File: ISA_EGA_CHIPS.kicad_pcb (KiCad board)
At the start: 2 copper layers, 131.1 x 108 mm, 67 parts, among them J1 EGA Feature Connector, J2 Light Pen, J3 RCA 1, J4 RCA 2, J6 Digital Output, J7 Bus_ISA_8bit, SW1 Configuration, U1 41464, U10 27C256, U11 82A436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

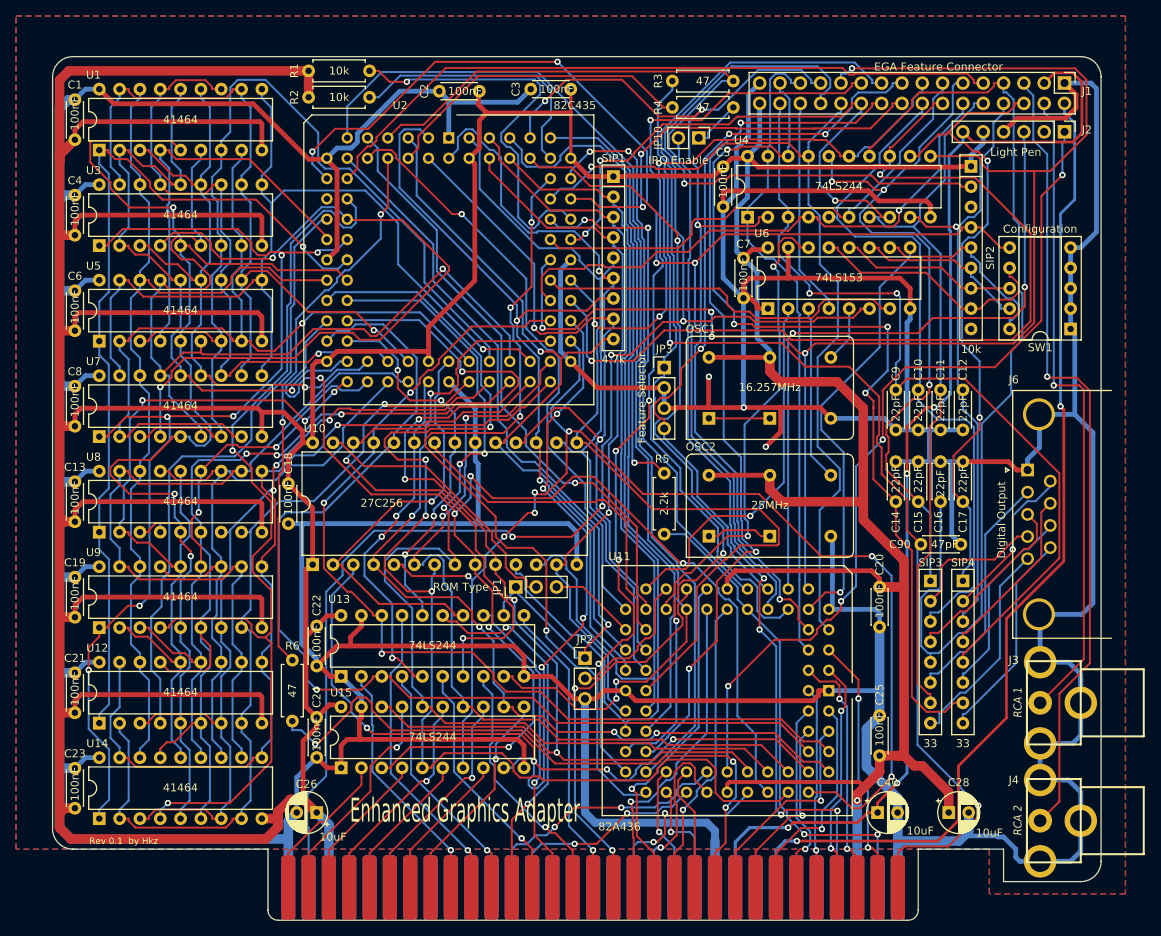
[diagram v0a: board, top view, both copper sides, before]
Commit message: Better ground plane
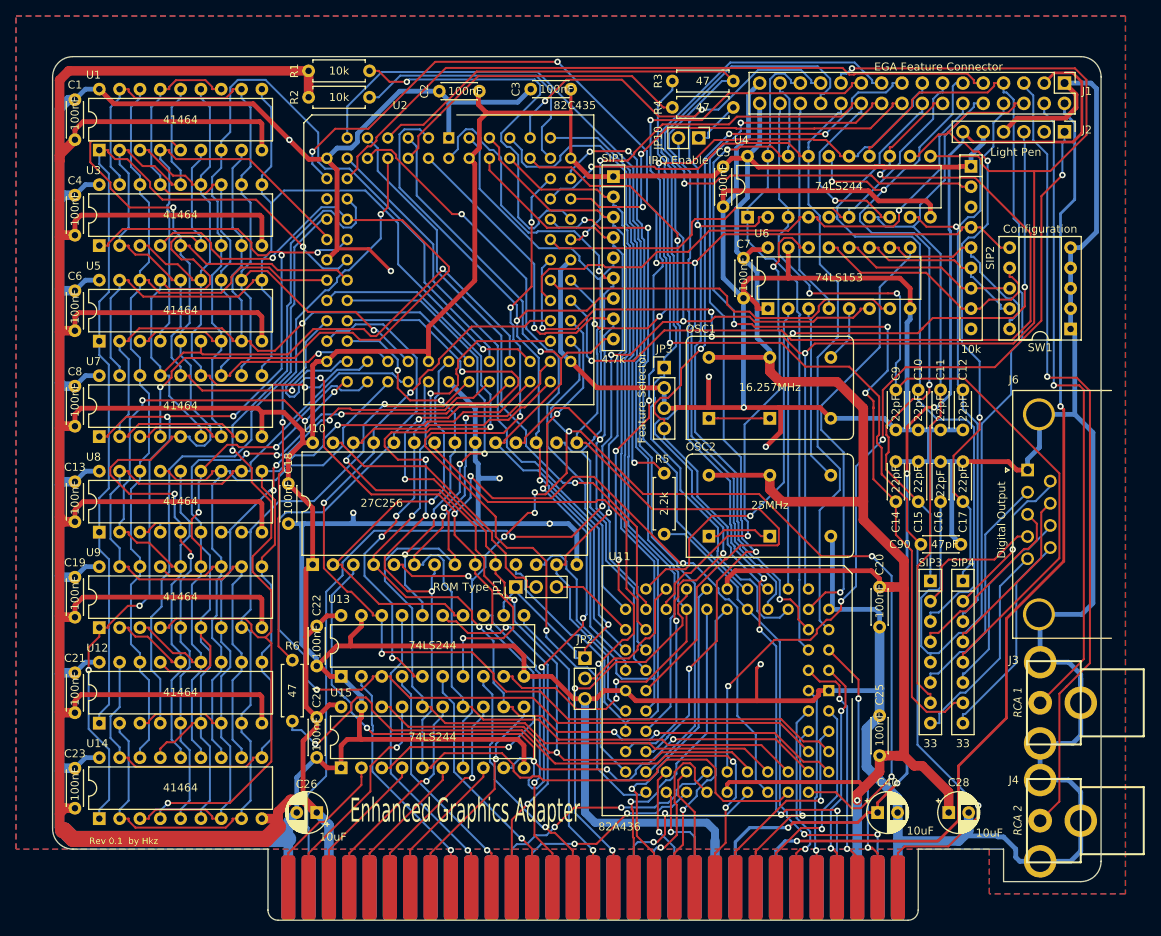
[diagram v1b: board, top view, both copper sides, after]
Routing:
- net VCC: track 809.4 -> 835.3 mm
- net GND: track 972.2 -> 992.4 mm, vias 3 -> 9
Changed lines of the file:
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@@
     (thickness 1.6)
     (drawings 22)
-    (tracks 4041)
+    (tracks 4069)
     (zones 0)
     (modules 67)
@@
   )
   (setup
-    (last_trace_width 0.25)
+    (last_trace_width 0.4)
     (user_trace_width 0.4)
     (user_trace_width 0.5)
@@
   (segment (start 189.738 99.568) (end 191.5664 101.3964) (width 0.6) (layer F.Cu) (net 1))
   (segment (start 191.5664 101.3964) (end 208.9802 101.3964) (width 0.6) (layer F.Cu) (net 1))
-  (segment (start 208.9802 101.3964) (end 215.9188 108.335) (width 0.6) (layer F.Cu) (net 1))
+  (segment (start 208.9802 101.3964) (end 213.4944 105.9106) (width 0.6) (layer F.Cu) (net 1))
   (segment (start 215.9188 108.335) (end 218.128 108.335) (width 0.6) (layer F.Cu) (net 1))
   (segment (start 218.128 108.335) (end 219.456 109.663) (width 0.6) (layer F.Cu) (net 1))
@@
   (segment (start 286.766 164.592) (end 281.3778 164.592) (width 0.6) (layer B.Cu) (net 1))
   (segment (start 236.7363 153.879) (end 237.0988 153.5165) (width 0.6) (layer B.Cu) (net 1))
-  (segment (start 237.0988 153.5165) (end 237.0988 146.3922) (width 0.6) (layer B.Cu) (net 1))
   (segment (start 237.0988 146.3922) (end 236.728 146.0214) (width 0.6) (layer B.Cu) (net 1))
   (segment (start 236.728 146.0214) (end 236.728 145.1143) (width 0.6) (layer B.Cu) (net 1))
@@
   (segment (start 214.416 185.604) (end 214.416 189.992) (width 0.6) (layer B.Cu) (net 1))
   (segment (start 255.524 174.752) (end 256.79 176.018) (width 0.6) (layer F.Cu) (net 1))
-  (segment (start 256.79 176.018) (end 278.9485 176.018) (width 0.6) (layer F.Cu) (net 1))
   (segment (start 278.9485 176.018) (end 279.6625 175.304) (width 0.6) (layer F.Cu) (net 1))
   (segment (start 279.6625 175.304) (end 279.6625 174.752) (width 0.6) (layer F.Cu) (net 1))
@@
   (segment (start 242.824 172.974) (end 244.1743 172.974) (width 0.6) (layer F.Cu) (net 1))
   (segment (start 236.728 143.764) (end 236.728 145.1143) (width 0.6) (layer B.Cu) (net 1))
-  (segment (start 215.3466 153.879) (end 236.7363 153.879) (width 0.6) (layer B.Cu) (net 1))
   (segment (start 213.36 153.879) (end 215.3466 153.879) (width 0.6) (layer B.Cu) (net 1))
   (segment (start 275.854 123.19) (end 289.814 123.19) (width 0.6) (layer F.Cu) (net 1))
@@
   (segment (start 271.9637 126.5337) (end 271.9637 127) (width 0.6) (layer F.Cu) (net 1))
   (segment (start 270.256 125.7) (end 270.256 124.826) (width 0.6) (layer F.Cu) (net 1))
-  (segment (start 236.7363 153.879) (end 248.367 153.879) (width 0.6) (layer B.Cu) (net 1))
+  (segment (start 236.7363 153.879) (end 246.044 153.879) (width 0.6) (layer B.Cu) (net 1))
   (segment (start 248.367 153.879) (end 249.428 154.94) (width 0.6) (layer B.Cu) (net 1))
   (segment (start 249.428 154.94) (end 249.428 159.004) (width 0.6) (layer B.Cu) (net 1))
@@
   (segment (start 189.738 99.568) (end 188.01 99.568) (width 0.6) (layer B.Cu) (net 1))
   (segment (start 188.01 99.568) (end 186.69 100.888) (width 0.6) (layer B.Cu) (net 1))
-  (segment (start 213.36 193.294) (end 186.182 193.294) (width 1.2) (layer B.Cu) (net 1))
   (segment (start 186.182 193.294) (end 184.771 191.883) (width 1.2) (layer B.Cu) (net 1))
   (segment (start 184.771 191.883) (end 184.771 184.799) (width 1.2) (layer B.Cu) (net 1))
@@
   (segment (start 279.8276 139.3656) (end 274.7476 139.3656) (width 0.6) (layer F.Cu) (net 1))
   (segment (start 274.7476 139.3656) (end 270.3026 139.3656) (width 0.6) (layer F.Cu) (net 1))
+  (via (at 221.488 152.527) (size 0.8) (drill 0.4) (layers F.Cu B.Cu) (net 1))
+  (via (at 239.776 148.209) (size 0.8) (drill 0.4) (layers F.Cu B.Cu) (net 1))
+  (segment (start 246.044 153.879) (end 248.367 153.879) (width 0.6) (layer B.Cu) (net 1))
+  (via (at 246.044 153.879) (size 0.8) (drill 0.4) (layers F.Cu B.Cu) (net 1))
+  (segment (start 221.488 152.527) (end 221.488 153.58) (width 0.6) (layer B.Cu) (net 1))
+  (segment (start 221.488 153.58) (end 221.189 153.879) (width 0.6) (layer B.Cu) (net 1))
+  (segment (start 221.189 153.879) (end 236.7363 153.879) (width 0.6) (layer B.Cu) (net 1))
+  (segment (start 215.3466 153.879) (end 221.189 153.879) (width 0.6) (layer B.Cu) (net 1))
+  (segment (start 237.363 148.209) (end 237.0988 147.9448) (width 0.6) (layer B.Cu) (net 1))
+  (segment (start 237.0988 147.9448) (end 237.0988 146.3922) (width 0.6) (layer B.Cu) (net 1))
+  (segment (start 239.776 148.209) (end 237.363 148.209) (width 0.6) (layer B.Cu) (net 1))
+  (segment (start 237.0988 153.5165) (end 237.0988 147.9448) (width 0.6) (layer B.Cu) (net 1))
+  (segment (start 211.348126 193.28899) (end 186.44852 193.28899) (width 2) (layer B.Cu) (net 1))
+  (segment (start 211.353136 193.294) (end 211.348126 193.28899) (width 2) (layer B.Cu) (net 1))
+  (segment (start 213.36 193.294) (end 211.353136 193.294) (width 2) (layer B.Cu) (net 1))
+  (segment (start 185.381375 192.221845) (end 185.186825 192.221845) (width 2) (layer B.Cu) (net 1))
+  (segment (start 186.44852 193.28899) (end 185.381375 192.221845) (width 2) (layer B.Cu) (net 1))
+  (segment (start 219.564799 119.525201) (end 223.411201 119.525201) (width 0.4) (layer F.Cu) (net 1))
+  (segment (start 218.186 120.904) (end 219.564799 119.525201) (width 0.4) (layer F.Cu) (net 1))
+  (segment (start 223.411201 119.525201) (end 226.187 122.301) (width 0.4) (layer F.Cu) (net 1))
+  (via (at 226.187 122.301) (size 0.8) (drill 0.4) (layers F.Cu B.Cu) (net 1))
+  (via (at 272.415 171.45) (size 0.8) (drill 0.4) (layers F.Cu B.Cu) (net 1))
+  (segment (start 271.903 171.962) (end 272.415 171.45) (width 0.4) (layer F.Cu) (net 1))
+  (segment (start 271.903 176.018) (end 271.903 171.962) (width 0.4) (layer F.Cu) (net 1))
+  (segment (start 256.79 176.018) (end 271.903 176.018) (width 0.6) (layer F.Cu) (net 1))
+  (segment (start 271.903 176.018) (end 278.9485 176.018) (width 0.6) (layer F.Cu) (net 1))
+  (segment (start 213.4944 105.9106) (end 215.9188 108.335) (width 0.6) (layer F.Cu) (net 1))
+  (via (at 213.4944 105.9106) (size 0.8) (drill 0.4) (layers F.Cu B.Cu) (net 1))
   (segment (start 297.3537 109.22) (end 297.2594 109.3143) (width 0.6) (layer F.Cu) (net 2))
   (segment (start 297.2594 109.3143) (end 287.7666 109.3143) (width 0.6) (layer F.Cu) (net 2))
@@
   (segment (start 212.09 191.77) (end 210.566 193.294) (width 1.2) (layer F.Cu) (net 2))
   (segment (start 210.566 193.294) (end 186.182 193.294) (width 1.2) (layer F.Cu) (net 2))
-  (segment (start 186.182 193.294) (end 184.771 191.883) (width 1.2) (layer F.Cu) (net 2))
   (segment (start 184.771 191.883) (end 184.771 190.105) (width 1.2) (layer F.Cu) (net 2))
   (segment (start 184.771 190.105) (end 184.771 177.405) (width 1.2) (layer F.Cu) (net 2))
@@
   (segment (start 212.792702 139.954) (end 215.138 142.299298) (width 0.6) (layer F.Cu) (net 2))
   (segment (start 210.058 139.954) (end 212.792702 139.954) (width 0.6) (layer F.Cu) (net 2))
+  (segment (start 210.57101 193.28899) (end 210.566 193.28899) (width 2) (layer F.Cu) (net 2))
+  (segment (start 212.09 191.77) (end 210.57101 193.28899) (width 2) (layer F.Cu) (net 2))
+  (segment (start 210.57101 193.28899) (end 186.44852 193.28899) (width 2) (layer F.Cu) (net 2))
+  (segment (start 185.381375 192.221845) (end 185.186825 192.221845) (width 2) (layer F.Cu) (net 2))
+  (segment (start 186.44852 193.28899) (end 185.381375 192.221845) (width 2) (layer F.Cu) (net 2))
   (segment (start 275.844 114.4447) (end 274.7187 113.3194) (width 0.25) (layer B.Cu) (net 3))
   (segment (start 274.7187 113.3194) (end 274.7187 102.6306) (width 0.25) (layer B.Cu) (net 3))

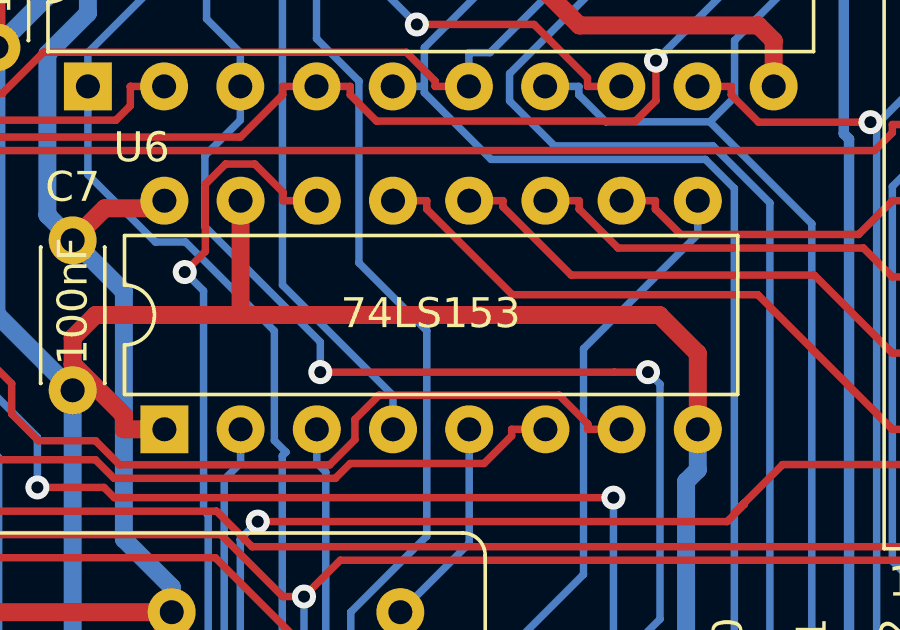
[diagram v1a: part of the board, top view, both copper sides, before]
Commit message: Some more vias
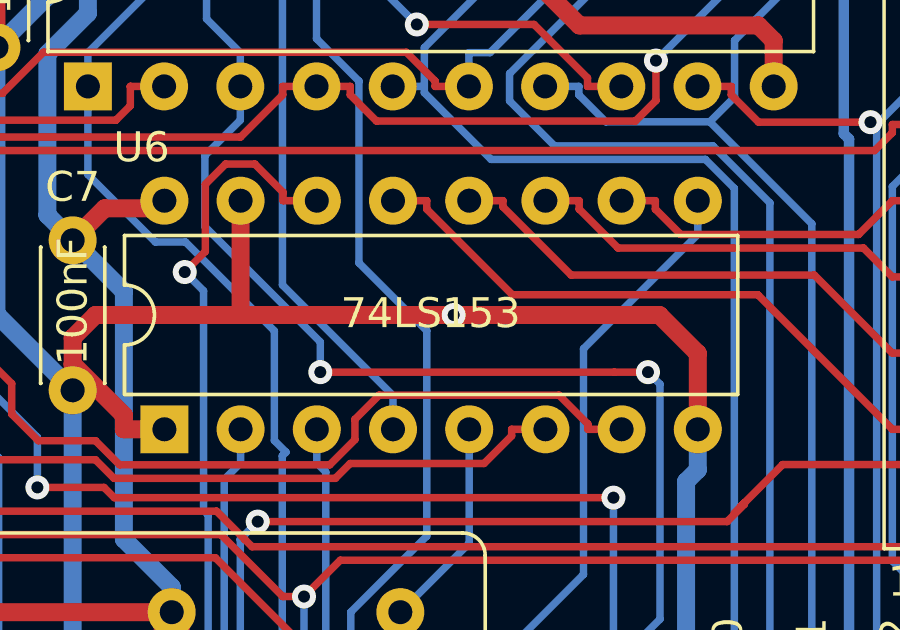
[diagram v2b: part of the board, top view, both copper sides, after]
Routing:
- net GND: vias 9 -> 10
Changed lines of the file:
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@@
     (thickness 1.6)
     (drawings 22)
-    (tracks 4069)
+    (tracks 4071)
     (zones 0)
     (modules 67)
@@
   (segment (start 236.728 143.764) (end 236.728 145.1143) (width 0.6) (layer B.Cu) (net 1))
   (segment (start 213.36 153.879) (end 215.3466 153.879) (width 0.6) (layer B.Cu) (net 1))
-  (segment (start 275.854 123.19) (end 289.814 123.19) (width 0.6) (layer F.Cu) (net 1))
+  (segment (start 275.854 123.19) (end 282.956 123.19) (width 0.6) (layer F.Cu) (net 1))
   (segment (start 289.814 123.19) (end 291.094 124.47) (width 0.6) (layer F.Cu) (net 1))
   (segment (start 291.094 124.47) (end 291.094 127) (width 0.6) (layer F.Cu) (net 1))
@@
   (segment (start 213.4944 105.9106) (end 215.9188 108.335) (width 0.6) (layer F.Cu) (net 1))
   (via (at 213.4944 105.9106) (size 0.8) (drill 0.4) (layers F.Cu B.Cu) (net 1))
+  (segment (start 282.956 123.19) (end 289.814 123.19) (width 0.6) (layer F.Cu) (net 1))
+  (via (at 282.956 123.19) (size 0.8) (drill 0.4) (layers F.Cu B.Cu) (net 1))
   (segment (start 297.3537 109.22) (end 297.2594 109.3143) (width 0.6) (layer F.Cu) (net 2))
   (segment (start 297.2594 109.3143) (end 287.7666 109.3143) (width 0.6) (layer F.Cu) (net 2))

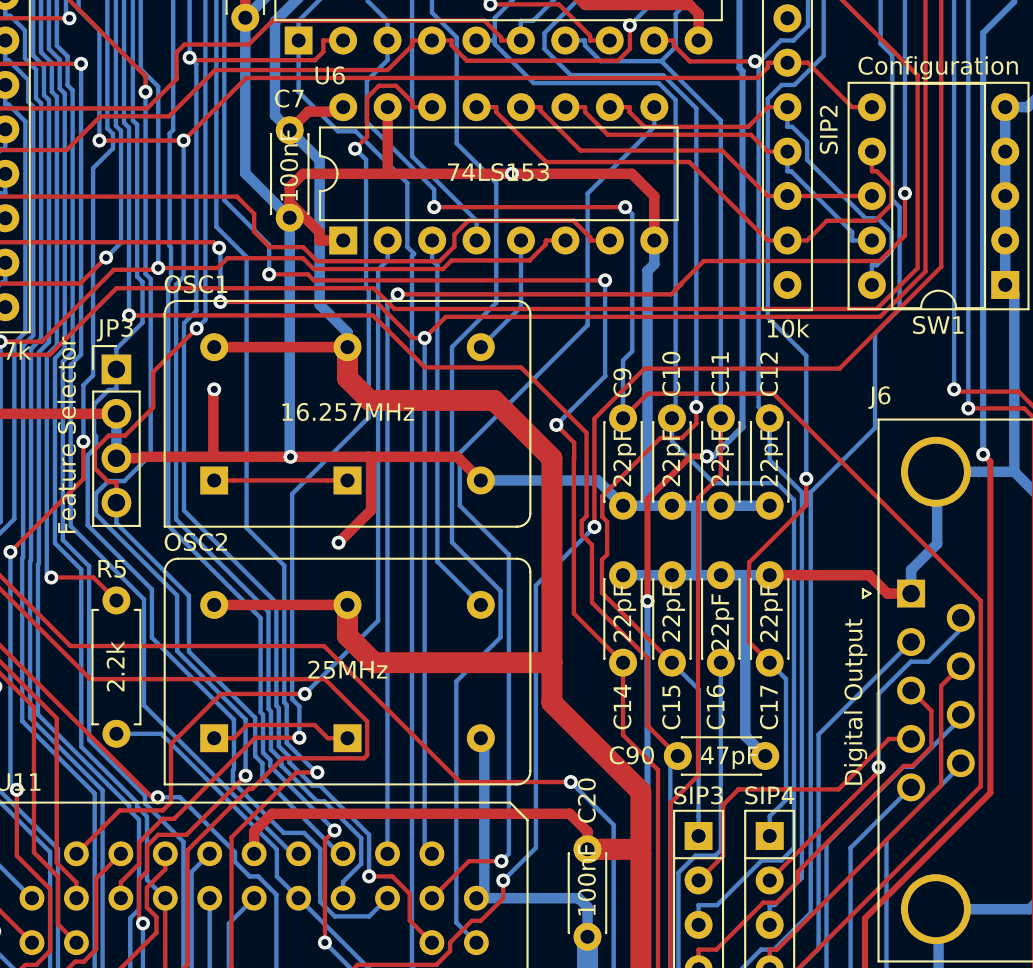
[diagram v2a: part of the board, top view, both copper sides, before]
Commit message: Add some more grounding
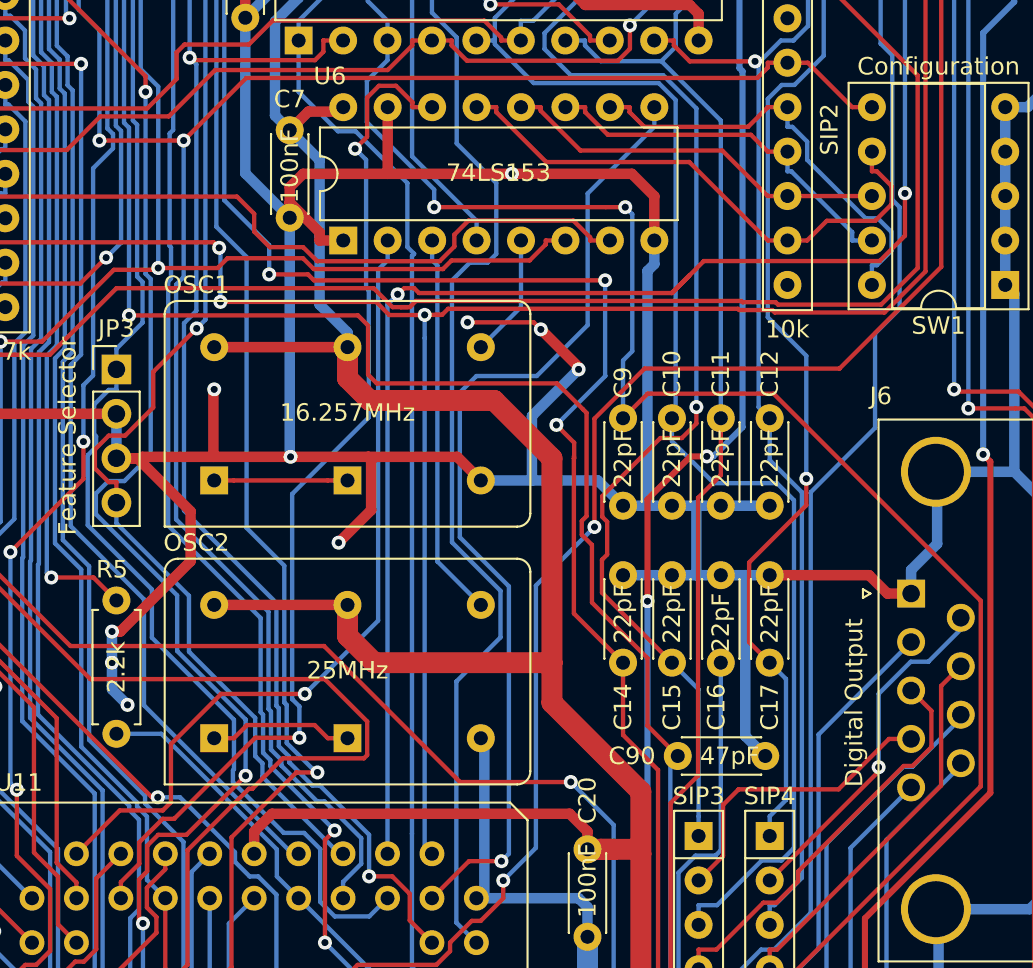
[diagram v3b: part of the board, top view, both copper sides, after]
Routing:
- net GND: track 992.4 -> 1026.4 mm, vias 10 -> 16
- net Net-(C90-Pad2): track 137.5 -> 139.8 mm
- net /SWITCH: track 53.9 -> 55.9 mm
- net /~LPENSW: track 85.2 -> 87.1 mm
- net /BS_V: track 187.8 -> 188.5 mm
- net /HIN: track 109.4 -> 110.0 mm
